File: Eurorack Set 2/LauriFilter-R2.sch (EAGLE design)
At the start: 42 parts, among them IC2 IC_74HC595-SOIC-16

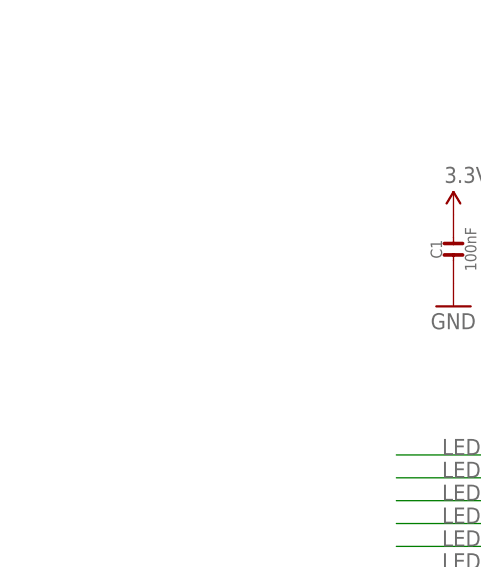
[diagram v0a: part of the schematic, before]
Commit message: Fiducials!
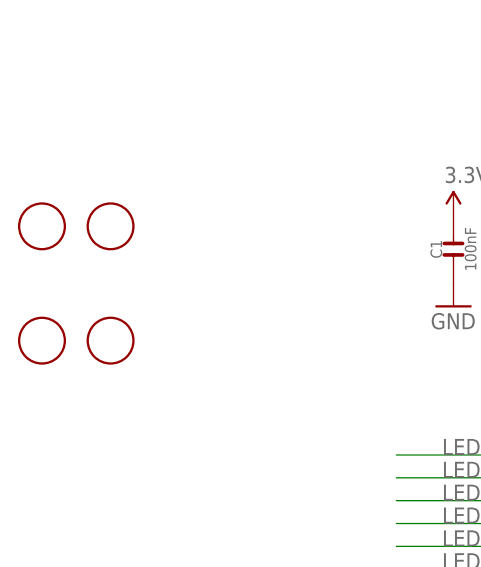
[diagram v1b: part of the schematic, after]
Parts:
- added U$15, U$16, U$17, U$18: FIDUCIAL, adafruit:FIDUCIAL
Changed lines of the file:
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@@
 <part name="R16" library="OPL" deviceset="R*" device="-0603" value="300"/>
 <part name="GND23" library="SparkFun-Aesthetics" deviceset="GND" device=""/>
+<part name="U$15" library="adafruit" deviceset="FIDUCIAL" device=""/>
+<part name="U$16" library="adafruit" deviceset="FIDUCIAL" device=""/>
+<part name="U$17" library="adafruit" deviceset="FIDUCIAL" device=""/>
+<part name="U$18" library="adafruit" deviceset="FIDUCIAL" device=""/>
 </parts>
 <sheets>
@@
 <instance part="R16" gate="R" x="115.57" y="-2.54" rot="R180"/>
 <instance part="GND23" gate="1" x="-7.62" y="86.36" rot="MR0"/>
+<instance part="U$15" gate="G$1" x="-81.28" y="132.08"/>
+<instance part="U$16" gate="G$1" x="-81.28" y="119.38"/>
+<instance part="U$17" gate="G$1" x="-73.66" y="132.08"/>
+<instance part="U$18" gate="G$1" x="-73.66" y="119.38"/>
 </instances>
 <busses>

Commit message: More tweaks
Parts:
- removed R13: 100k, OPL:R-0603
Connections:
- removed net N$10: R13.2, U$14.A
- net N$7: now also U$14.A; no longer R13.1
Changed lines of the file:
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@@
 <part name="SUPPLY2" library="SparkFun-Aesthetics" deviceset="3.3V" device=""/>
 <part name="SUPPLY5" library="SparkFun-Aesthetics" deviceset="3.3V" device=""/>
-<part name="R13" library="OPL" deviceset="R*" device="-0603" value="100k"/>
 <part name="R14" library="OPL" deviceset="R*" device="" value="300"/>
 <part name="R15" library="OPL" deviceset="R*" device="" value="300"/>
@@
 <instance part="SUPPLY2" gate="G$1" x="-27.94" y="142.24"/>
 <instance part="SUPPLY5" gate="G$1" x="-35.56" y="133.35"/>
-<instance part="R13" gate="R" x="-39.37" y="35.56"/>
 <instance part="R14" gate="R" x="86.36" y="22.86"/>
 <instance part="R15" gate="R" x="86.36" y="20.32"/>
@@
 <segment>
 <pinref part="U$4" gate="G$1" pin="TIP"/>
-<pinref part="R13" gate="R" pin="1"/>
-<wire x1="-43.18" y1="35.56" x2="-50.8" y2="35.56" width="0.1524" layer="91"/>
+<pinref part="U$14" gate="G$1" pin="A"/>
+<wire x1="-50.8" y1="35.56" x2="-27.94" y2="35.56" width="0.1524" layer="91"/>
 </segment>
 </net>
@@
 </segment>
 </net>
-<net name="N$10" class="0">
-<segment>
-<pinref part="U$14" gate="G$1" pin="A"/>
-<wire x1="-27.94" y1="35.56" x2="-35.56" y2="35.56" width="0.1524" layer="91"/>
-<pinref part="R13" gate="R" pin="2"/>
-</segment>
-</net>
